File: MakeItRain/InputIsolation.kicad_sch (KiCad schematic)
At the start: 21 parts, among them IC2 LTV-846S, Q14 BS250, Q15 BS250, Q16 BS250, Q17 BS250

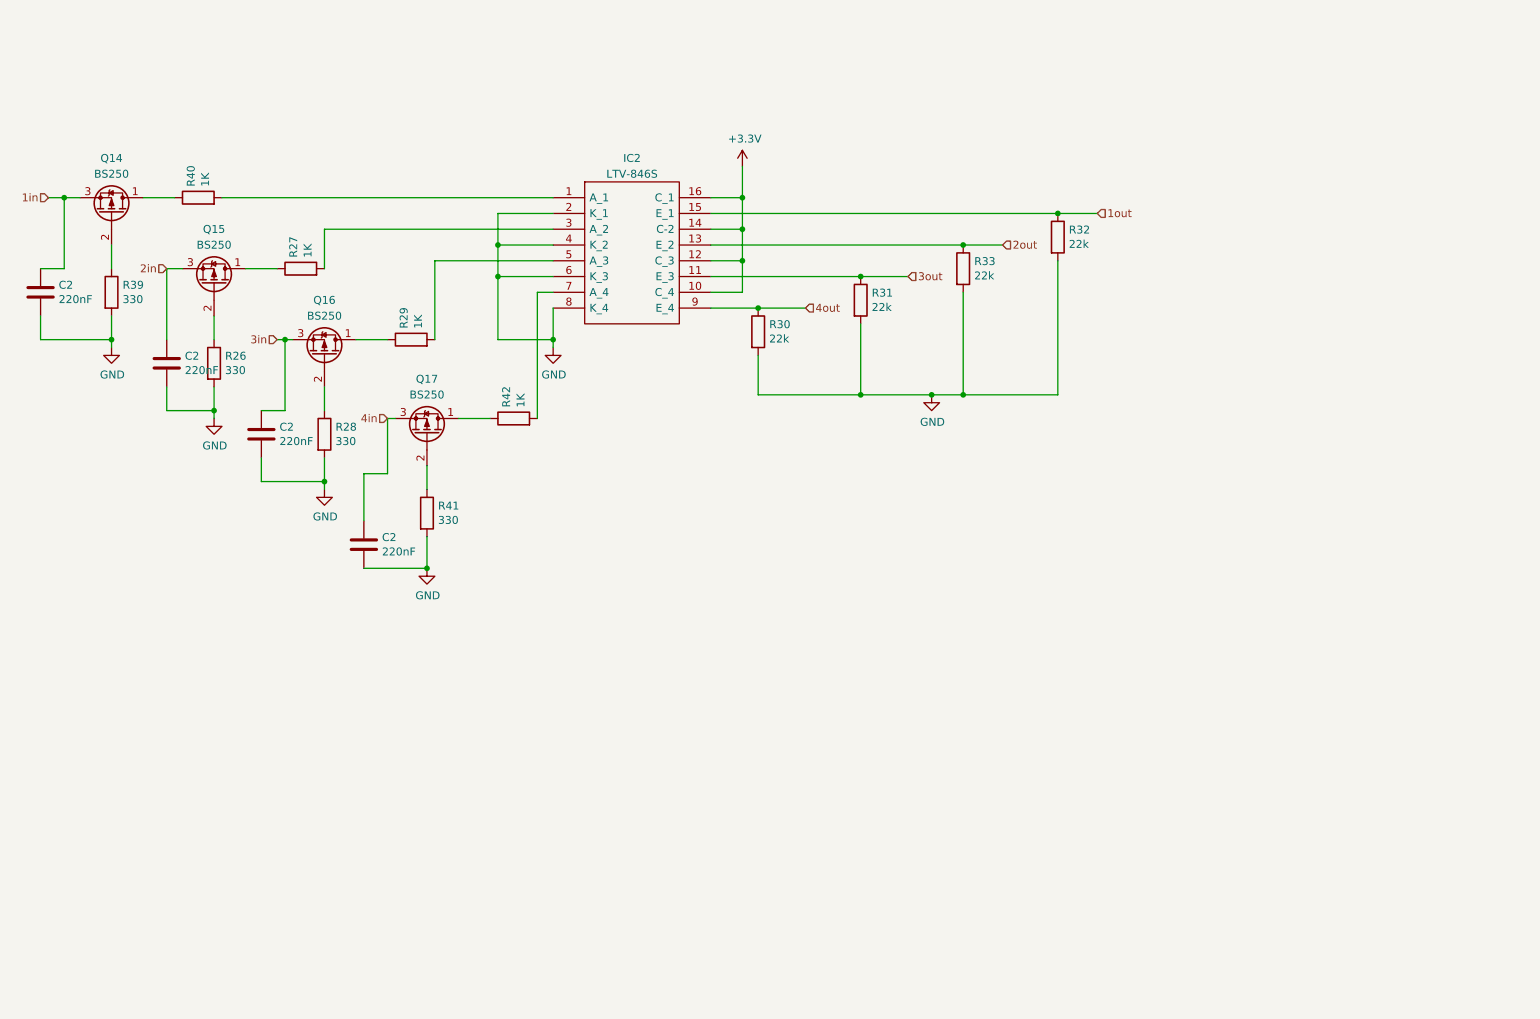
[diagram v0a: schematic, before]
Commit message: * updated InputIsolation.kicad_sch to have the N channel Fet for Input impedance * added to the PCB but haven't placed or routed
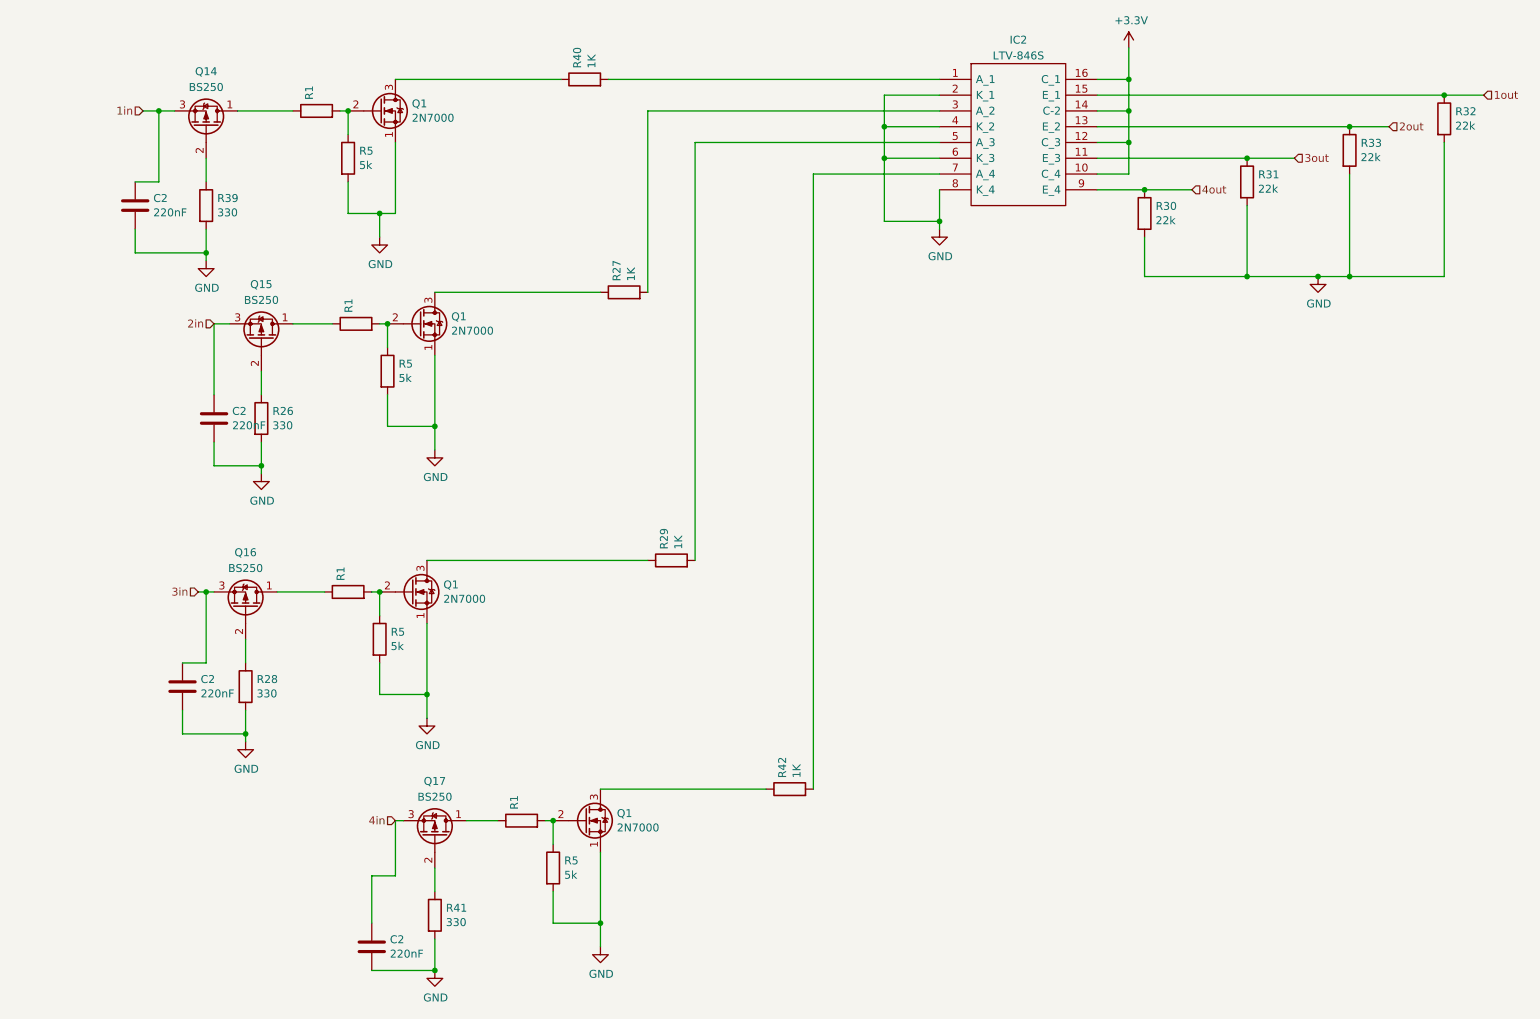
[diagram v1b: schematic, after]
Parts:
- added Q1 (x4): 2N7000, Package_TO_SOT_THT:TO-92_Inline, symbol Transistor_FET:2N7000
- added R1 (x4): 470, Resistor_THT:R_Axial_DIN0207_L6.3mm_D2.5mm_P2.54mm_Vertical, symbol Device:R
- added R5 (x4): 5k, Resistor_THT:R_Axial_DIN0207_L6.3mm_D2.5mm_P2.54mm_Vertical, symbol Device:R
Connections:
- net GND: now also Q1.1 (S), Q1.1 (S), Q1.1 (S), Q1.1 (S), R5.2, R5.2, R5.2, R5.2
- net at R40.1: now also Q1.3 (D); no longer Q14.1 (D)
- net at R27.1: now also Q1.3 (D); no longer Q15.1 (D)
- net at Q16.1 (D): now also R1.1; no longer R29.1
- net at Q17.1 (D): now also R1.1; no longer R42.1
- new net: Q1.2 (G), R1.2, R5.1 (x4)
- new net: Q14.1 (D), R1.1
- new net: Q1.3 (D), R42.1
- new net: Q1.3 (D), R29.1
- new net: Q15.1 (D), R1.1
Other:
- moved on the sheet: C2, IC2, Q14, Q15, Q16, Q17, R26, R27, R28, R29, R30, R31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
